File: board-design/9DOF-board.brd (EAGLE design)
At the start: 102.5 x 74.9 mm, 14 parts

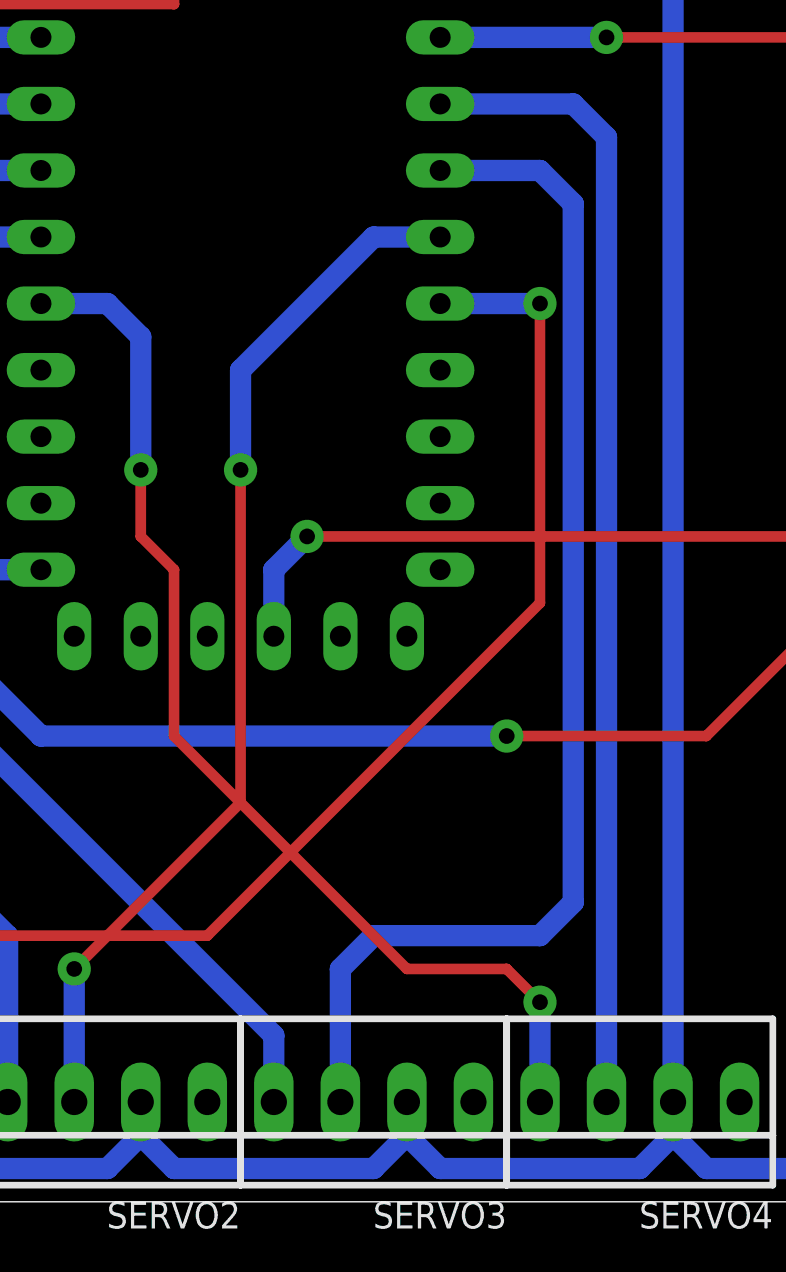
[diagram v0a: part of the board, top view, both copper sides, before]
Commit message: fixed clearance error
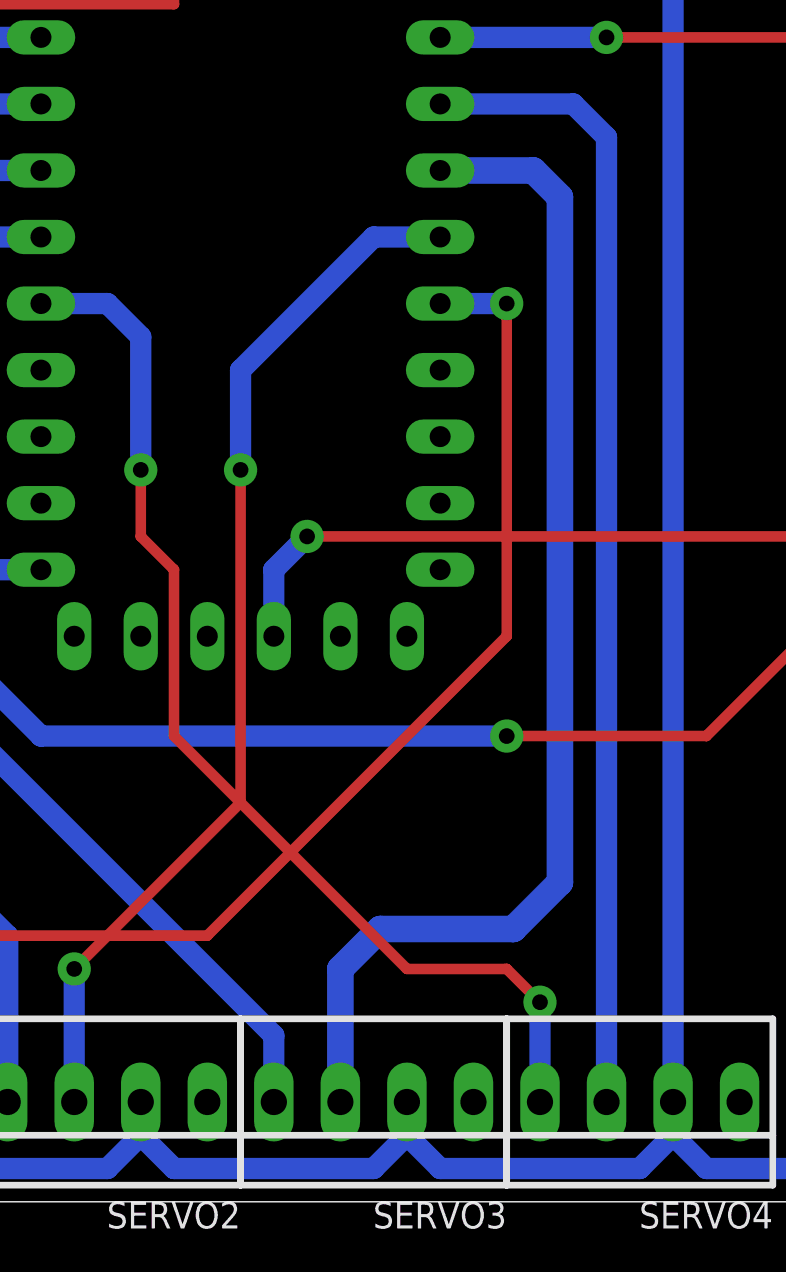
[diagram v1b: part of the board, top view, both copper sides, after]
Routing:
- net SERVO1_SIG: track 54.8 -> 53.0 mm
- net SERVO3_SIG: track 47.3 -> 46.0 mm
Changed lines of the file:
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@@
 <setting verticaltext="up"/>
 </settings>
-<grid distance="0.05" unitdist="inch" unit="inch" style="lines" multiple="1" display="no" altdistance="0.025" altunitdist="inch" altunit="inch"/>
+<grid distance="0.01" unitdist="inch" unit="inch" style="lines" multiple="1" display="no" altdistance="0.025" altunitdist="inch" altunit="inch"/>
 <layers>
 <layer number="1" name="Top" color="4" fill="1" visible="yes" active="yes"/>
@@
 <signal name="SERVO3_SIG">
 <contactref element="U$1" pad="D4"/>
-<wire x1="33.02" y1="11.43" x2="33.02" y2="38.1" width="0.8128" layer="16"/>
-<wire x1="33.02" y1="38.1" x2="31.75" y2="39.37" width="0.8128" layer="16"/>
-<wire x1="31.75" y1="39.37" x2="27.94" y2="39.37" width="0.8128" layer="16"/>
 <contactref element="SERVO3" pad="3"/>
-<wire x1="33.02" y1="11.43" x2="31.75" y2="10.16" width="0.8128" layer="16"/>
-<wire x1="31.75" y1="10.16" x2="25.4" y2="10.16" width="0.8128" layer="16"/>
-<wire x1="25.4" y1="10.16" x2="24.13" y2="8.89" width="0.8128" layer="16"/>
-<wire x1="24.13" y1="8.89" x2="24.13" y2="3.81" width="0.8128" layer="16"/>
+<wire x1="27.94" y1="39.37" x2="31.496" y2="39.37" width="1.016" layer="16"/>
+<wire x1="31.496" y1="39.37" x2="32.512" y2="38.354" width="1.016" layer="16"/>
+<wire x1="32.512" y1="38.354" x2="32.512" y2="12.192" width="1.016" layer="16"/>
+<wire x1="32.512" y1="12.192" x2="30.734" y2="10.414" width="1.016" layer="16"/>
+<wire x1="30.734" y1="10.414" x2="25.654" y2="10.414" width="1.016" layer="16"/>
+<wire x1="25.654" y1="10.414" x2="24.13" y2="8.89" width="1.016" layer="16"/>
+<wire x1="24.13" y1="8.89" x2="24.13" y2="3.81" width="1.016" layer="16"/>
 </signal>
 <signal name="SERVO4_SIG">
@@
 <via x="3.81" y="10.16" extent="1-16" drill="0.6" diameter="1.27" shape="square"/>
 <wire x1="3.81" y1="10.16" x2="19.05" y2="10.16" width="0.4064" layer="1"/>
-<wire x1="19.05" y1="10.16" x2="31.75" y2="22.86" width="0.4064" layer="1"/>
-<wire x1="31.75" y1="22.86" x2="31.75" y2="34.29" width="0.4064" layer="1"/>
-<via x="31.75" y="34.29" extent="1-16" drill="0.6" diameter="1.27" shape="square"/>
-<wire x1="31.75" y1="34.29" x2="27.94" y2="34.29" width="0.8128" layer="16"/>
+<wire x1="19.05" y1="10.16" x2="30.48" y2="21.59" width="0.4064" layer="1"/>
+<wire x1="30.48" y1="21.59" x2="30.48" y2="34.29" width="0.4064" layer="1"/>
+<via x="30.48" y="34.29" extent="1-16" drill="0.6" diameter="1.27" shape="square"/>
+<wire x1="30.48" y1="34.29" x2="27.94" y2="34.29" width="0.8128" layer="16"/>
 <contactref element="SERVO1" pad="3"/>
 <wire x1="3.81" y1="3.81" x2="3.81" y2="10.16" width="0.8128" layer="16"/>
